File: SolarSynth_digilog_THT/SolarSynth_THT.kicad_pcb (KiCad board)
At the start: 2 copper layers, 60 x 89 mm, 32 parts, among them J1 OutputJack1, J2 Conn_01x01_Pin, J3 Conn_01x01_Pin, P1 PiezoDisc, P2 PiezoDisc, U1 74HC14, U2 MCP6002-xMC

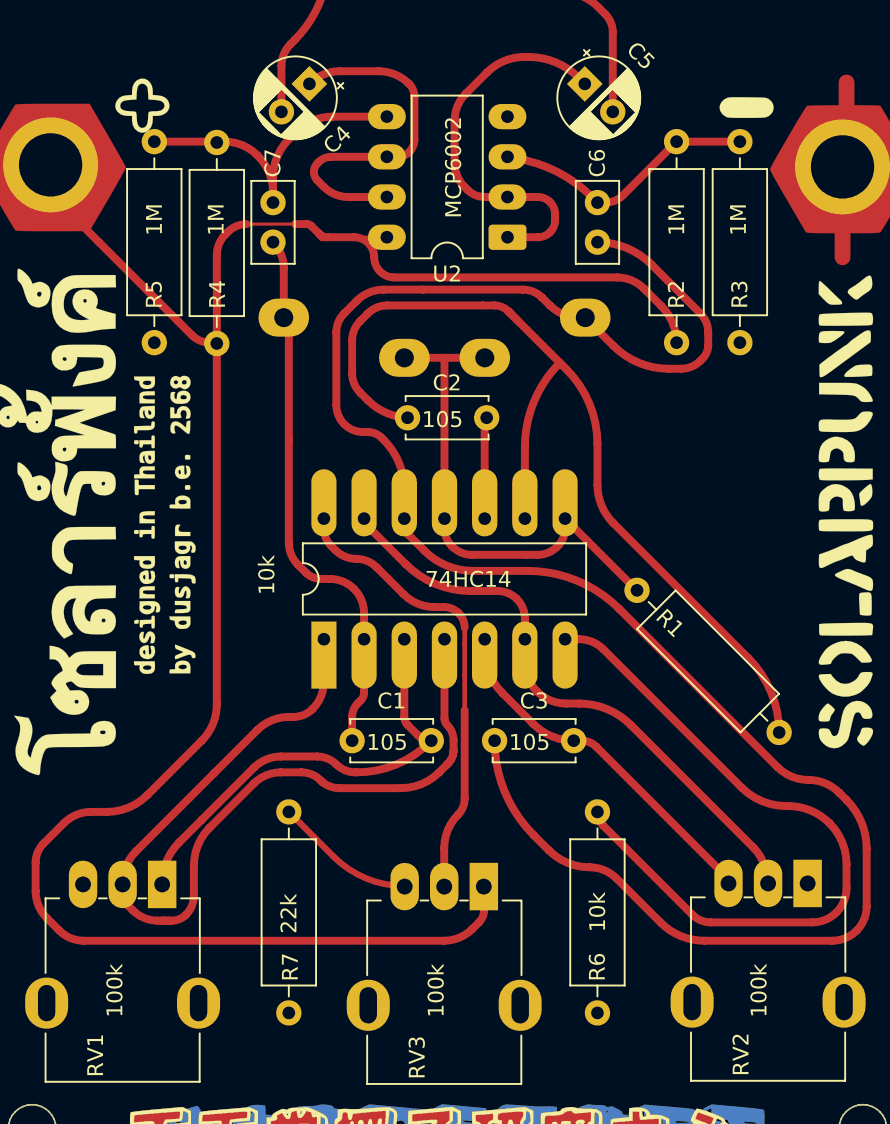
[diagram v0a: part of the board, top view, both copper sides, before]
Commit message: fixed some errors. Made it easier to solder and added blinkyparts logo
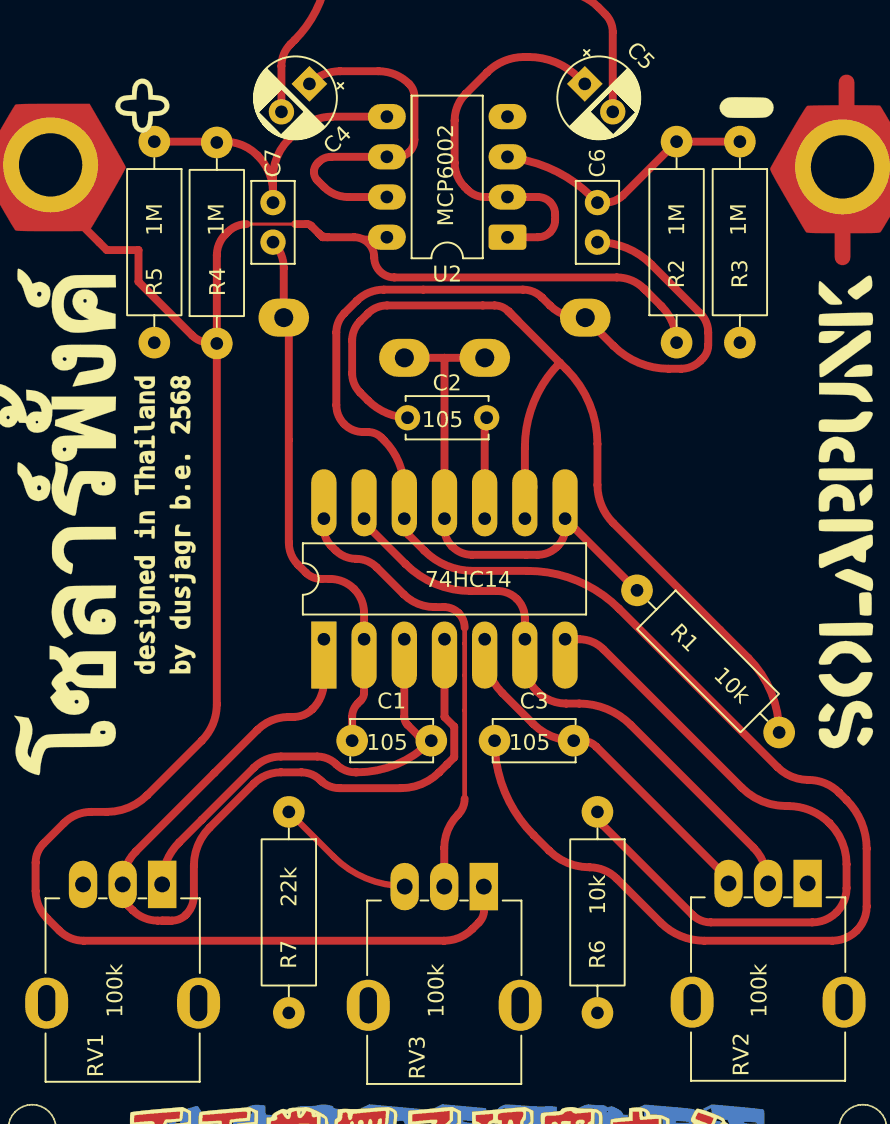
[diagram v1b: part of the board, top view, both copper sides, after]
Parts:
- added blinkyparts_logo_15mm: G***, blinkyparts:logo_15mm, F.Cu at (91.5, 33.5)
- C1, C3: footprint Capacitor_THT:C_Disc_D5.0mm_W2.5mm_P5.00mm -> blinkyparts:C_Disc_D5.0mm_W2.5mm_P5.00mm_handsoldering
- R1, R2, R3, R4, R5, R6, R7: footprint Resistor_THT:R_Axial_DIN0309_L9.0mm_D3.2mm_P12.70mm_Horizontal -> blinkyparts:R_Axial_DIN0309_L9.0mm_D3.2mm_P12.70mm_Horizontal_handsoldering
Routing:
- net VCC: track 125.0 -> 126.2 mm
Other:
- board text added: "blinkyparts GmbH Egerstr. 9 93057 Regensburg Version 1.2 - THT"
- board text removed: "blinkyparts GmbH Egerstr. 9 93057 Regensburg Version 1.1 - THT"
